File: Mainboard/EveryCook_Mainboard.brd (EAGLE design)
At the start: 103.1 x 86.4 mm, 104 parts, among them IC1 LM386MM-1, IC2 ATMEGA644A, Q1 8 MHz, Q2 BSP372, Q3 BSP372, T2 ZDT6790, U1 AD7794BRUZ, U4 78M05, U7 CJ1117-3.3

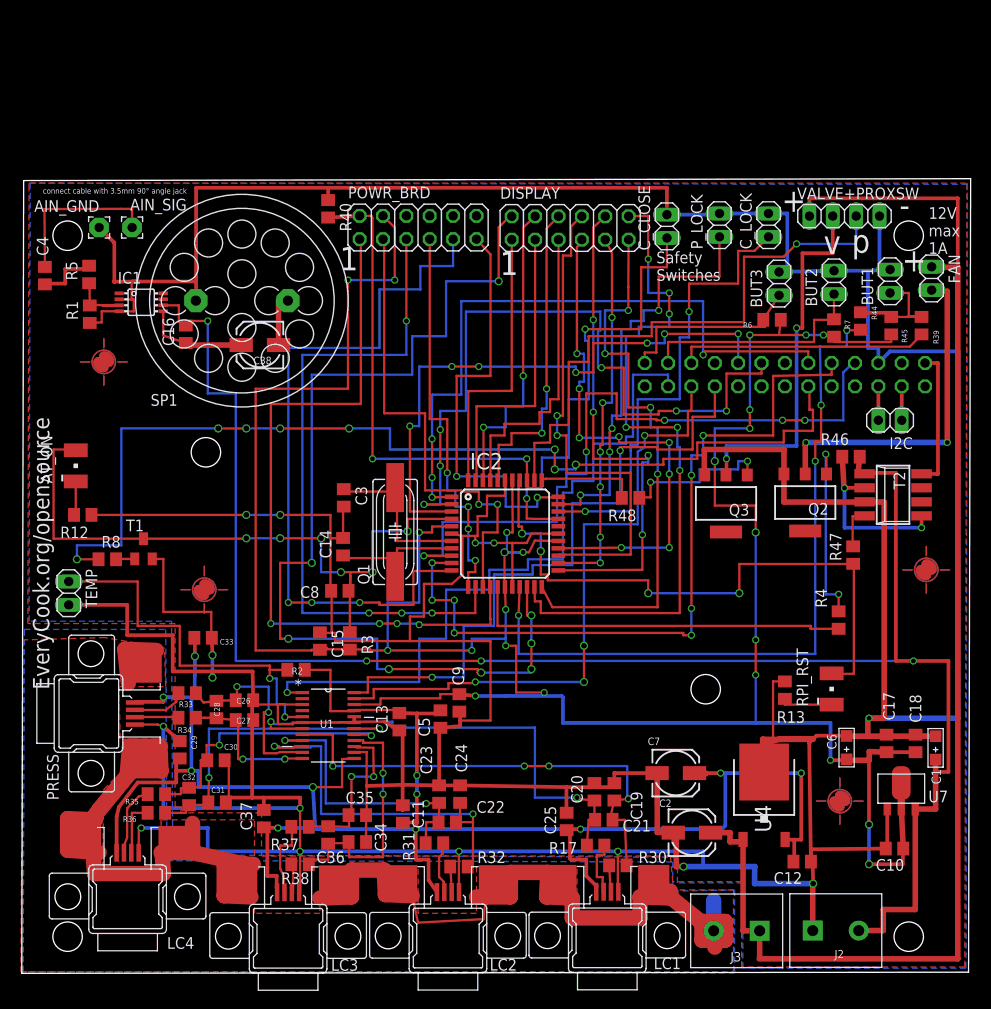
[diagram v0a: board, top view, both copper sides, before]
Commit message: Changed USB connectors, created gerber Files
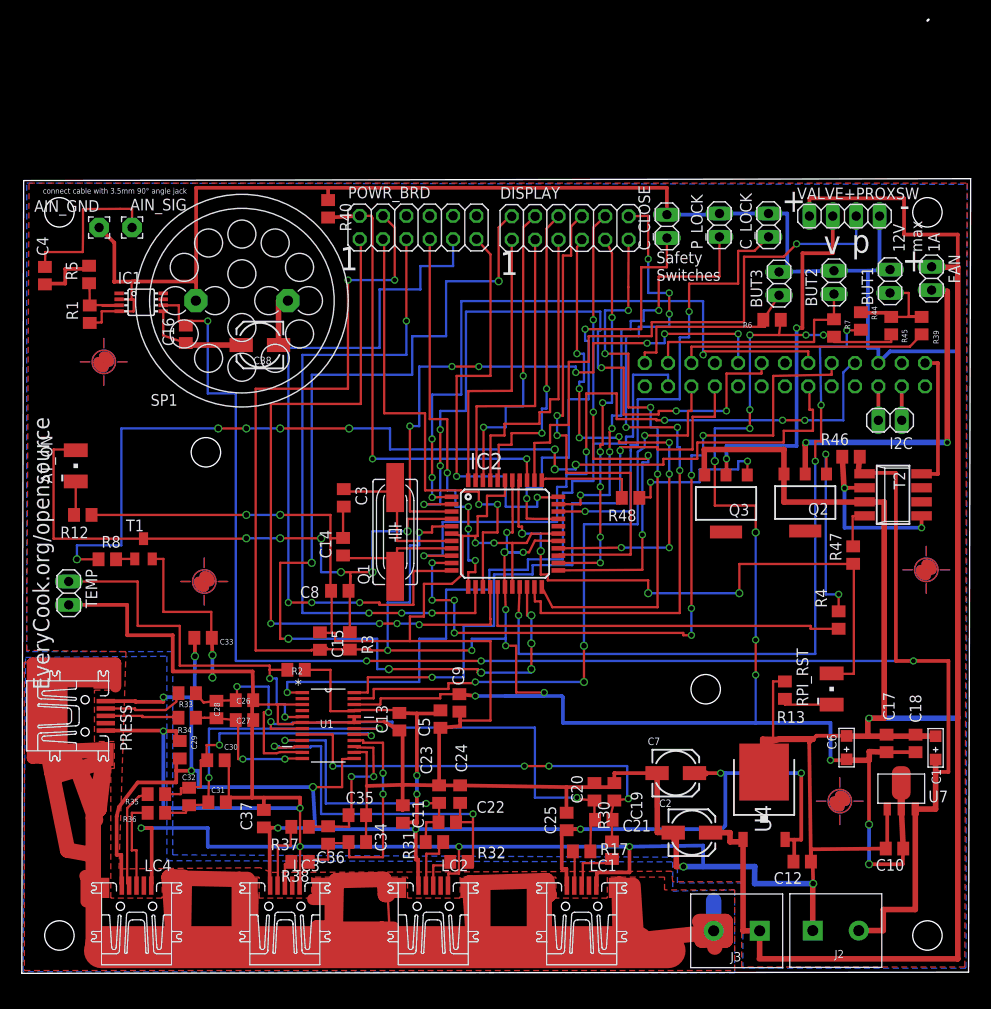
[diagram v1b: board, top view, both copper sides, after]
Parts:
- LC1, LC2, LC3, LC4, PRESS: value MINI-USB_4P-85-32006-601-1 -> MINI-USB-SHIELD-UX60-MB-5ST; device con-cypressindustries:85-32006-601-1 -> con-hirose:UX60-MB-5ST
- moved LC1 4.25 mm to (61.0, 3.30), turned to 90 degrees
- moved LC2 3.60 mm to (44.8, 3.30), turned to 90 degrees
- moved LC3 3.27 mm to (28.7, 3.30), turned to 90 degrees
- moved R30 1.77 mm to (64.3, 9.40), turned to 270 degrees
- moved R17 1.65 mm to (61.0, 9.27), turned to 180 degrees
- moved LC4 1.42 mm to (12.6, 3.30), turned to 90 degrees
- moved U$2 0.89 mm to (19.9, 38.6)
- moved PRESS 0.68 mm to (6.99, 24.0), turned to 0 degrees
- moved R32 0.51 mm to (47.6, 8.13)
- moved R38 0.25 mm to (30.4, 8.13)
- moved R31 0.13 mm to (45.0, 10.3)
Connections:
- net N$55 renamed AT_MISO
- net N$56 renamed AT_MOSI
- net N$8 renamed SCK
- net GND: now also LC1.5, LC2.5, LC3.5, LC4.5, PRESS.5; no longer LC1.4, LC2.4, LC3.4, LC4.4, PRESS.4
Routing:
- net PGND: track 164.9 -> 474.3 mm
- net GND: track 773.3 -> 784.8 mm
- net LOADCELL4_SIG-: track 6.12 -> 10.2 mm
- net N$48: track 52.7 -> 48.8 mm
- net LOADCELL4_SIG+: track 7.71 -> 11.3 mm
- net LOADCELL1_SIG-: track 2.90 -> 6.34 mm
- net PRESS_SIG+: track 5.79 -> 9.10 mm
- net PRESS_SIG-: track 4.80 -> 8.09 mm
- net LOADCELL1_SIG+: track 6.60 -> 3.95 mm
- net L5V: track 207.0 -> 209.1 mm
- net LOADCELL2_SIG-: track 2.81 -> 4.42 mm
- net LOADCELL3_SIG+: track 8.62 -> 7.85 mm
- net LOADCELL2_SIG+: track 5.74 -> 6.30 mm
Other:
- board size 103.1 x 86.4 mm -> 103.1 x 103.7 mm

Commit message: Redesign of all boards.
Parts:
- removed AIN_GND, AIN_SIG: (no value), wirepad:2,15/1,0
- removed BUT2, BUT3, C_CLOSE, P_LOCK: (no value), pinhead:1X02
- removed RASPI_CONNECTOR_(TOP): (no value), pinhead:2X13
- added AIN: (no value), pinhead:1X02
- added BUT2+3, CO_CL+PU_LK: (no value), pinhead:1X03
- added R9: 270, rcl:R0805
- added T3: (no value), transistor:SOT23-BEC
- added U$5: RPI-B-V2, raspberry_mirr:RPI-B-V2
- moved AT_ON 82.7 mm to (88.1, 61.0)
- moved R12 82.0 mm to (88.0, 56.5), turned to 0 degrees
- moved R8 77.4 mm to (83.1, 64.9), turned to 270 degrees
- moved T1 73.3 mm to (84.2, 61.0), turned to 270 degrees
- moved R4 57.1 mm to (47.2, 73.5)
- moved FAN 55.3 mm to (44.2, 79.2), turned to 180 degrees
- moved C_LOCK 55.0 mm to (26.3, 78.7)
- moved Q2 49.8 mm to (42.5, 72.6)
- moved C14 40.4 mm to (75.3, 46.1), turned to 0 degrees
- moved C3 40.4 mm to (75.2, 42.8), turned to 0 degrees
- moved U$3 29.6 mm to (60.7, 23.4)
- moved Q1 28.2 mm to (68.8, 46.3), turned to 270 degrees
- moved C8 28.1 mm to (62.7, 36.6)
- moved POWR_BRD 28.0 mm to (15.2, 78.7)
- moved C15 24.7 mm to (57.1, 33.4)
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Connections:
- removed net IH_OFF: IC2.11, POWR_BRD.9
- removed net N$12: I2C.2, RASPI_CONNECTOR_(TOP).3
- removed net N$15: DISPLAY.11, IC2.22
- removed net N$16: DISPLAY.10, IC2.23
- removed net N$17: DISPLAY.9, IC2.24
- removed net N$18: DISPLAY.8, IC2.25
- removed net N$19: DISPLAY.7, IC2.26
- removed net N$37: DISPLAY.6, IC2.40
- removed net N$38: DISPLAY.5, IC2.41
- removed net N$39: DISPLAY.4, IC2.42
- removed net N$41: DISPLAY.3, IC2.43
- removed net N$43: DISPLAY.1, IC2.44
- removed net N$50: I2C.1, RASPI_CONNECTOR_(TOP).5
- removed net N$59: C_CLOSE.1, IC2.30
- removed net N$61: IC2.32, P_LOCK.1
- new net C_CLOSE: CO_CL+PU_LK.1, IC2.30
- new net N$6: I2C.2, U$5.P1_3
- new net N$8: POWR_BRD.12, T3.C
- new net PB0: DISPLAY.1, IC2.40
- new net PB1: DISPLAY.2, IC2.41
- new net PB2: DISPLAY.3, IC2.42
- new net PB3: DISPLAY.4, IC2.43
- new net PC0: DISPLAY.5, IC2.19
- new net PC1: DISPLAY.6, IC2.20
- new net PC2: DISPLAY.7, IC2.21
- new net PC3: DISPLAY.8, IC2.22
- new net PC4: DISPLAY.9, IC2.23
- new net PC5: DISPLAY.10, IC2.24
- new net PC6: DISPLAY.11, IC2.25
- new net PC7: DISPLAY.12, IC2.26
- new net P_LOCK: CO_CL+PU_LK.2, IC2.32
- net +3V3: now also IC2.29
- net +5V: now also POWR_BRD.11
- net AT_MISO: now also U$5.P1_16; no longer RASPI_CONNECTOR_(TOP).16
- net AT_MOSI: now also U$5.P1_12; no longer RASPI_CONNECTOR_(TOP).12
- net DAEMON_RST_LINE: now also IC2.11; no longer IC2.19
- net GND: now also AIN.1, BUT2+3.3, CO_CL+PU_LK.3, IC2.44, T3.E, U$5.P1_14, U$5.P1_20, U$5.P1_25, U$5.P1_6; no longer AIN_GND.1, BUT2.2, BUT3.2, C_CLOSE.2, P_LOCK.2, RASPI_CONNECTOR_(TOP).6
- net MISO: now also U$5.P1_21; no longer RASPI_CONNECTOR_(TOP).21
- net MOSI: now also U$5.P1_19; no longer RASPI_CONNECTOR_(TOP).19
- net N$1: now also I2C.1, U$5.P1_5; no longer DISPLAY.2, IC2.20
- net N$11: now also R9.1, T3.B; no longer DISPLAY.12, IC2.21
- net N$27: now also AIN.2; no longer AIN_SIG.1
- net N$52: now also U$5.P1_8; no longer RASPI_CONNECTOR_(TOP).8
- net N$54: now also U$5.P1_10; no longer RASPI_CONNECTOR_(TOP).10
- net N$58: now also U$5.P1_2, U$5.P1_4; no longer RASPI_CONNECTOR_(TOP).2
- net N$62: now also BUT2+3.1, U$5.P1_26; no longer BUT2.1, RASPI_CONNECTOR_(TOP).24
- net N$63: now also BUT2+3.2, U$5.P1_24; no longer BUT3.1, RASPI_CONNECTOR_(TOP).26
- net N$64: now also U$5.P1_22; no longer RASPI_CONNECTOR_(TOP).22
- net RPI_ATMEL_RST: now also U$5.P1_11; no longer RASPI_CONNECTOR_(TOP).11
- net SAFETY_CHAIN: now also R9.2; no longer POWR_BRD.11
- net SCK: now also U$5.P1_18; no longer RASPI_CONNECTOR_(TOP).18
- net SCLK: now also U$5.P1_23; no longer RASPI_CONNECTOR_(TOP).23
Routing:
- net RPI_ATMEL_RST: track 110.6 -> 4.00 mm, vias 8 -> 0
- net N$1: track 111.2 -> 25.0 mm, vias 8 -> 0
- net IH_OFF: track 79.1 -> 0.00 mm, vias 3 -> 0
- net N$11: track 76.7 -> 8.73 mm, vias 6 -> 0
- net PB1: track 0.00 -> 66.5 mm, vias 0 -> 1
- net N$15: track 62.1 -> 0.00 mm, vias 4 -> 0
- net PC7: track 0.00 -> 61.1 mm
- net PB3: track 0.00 -> 61.1 mm, vias 0 -> 1
- net PB0: track 0.00 -> 59.4 mm, vias 0 -> 1
- net PC5: track 0.00 -> 59.1 mm, vias 0 -> 4
- net P_LOCK: track 0.00 -> 57.6 mm, vias 0 -> 3
- net N$19: track 56.9 -> 0.00 mm, vias 8 -> 0
- net C_CLOSE: track 0.00 -> 55.6 mm, vias 0 -> 3
- net N$16: track 55.5 -> 0.00 mm, vias 4 -> 0
- net N$18: track 54.8 -> 0.00 mm, vias 2 -> 0
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- added copper zone on layer 1, net GND
- added copper zone on layer 16, net GND
- removed copper zone on layer 16, net N$21
- removed copper zone on layer 1, net N$28
